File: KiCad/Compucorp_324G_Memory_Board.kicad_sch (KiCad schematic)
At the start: 1 part, among them J10 Memory Interboard

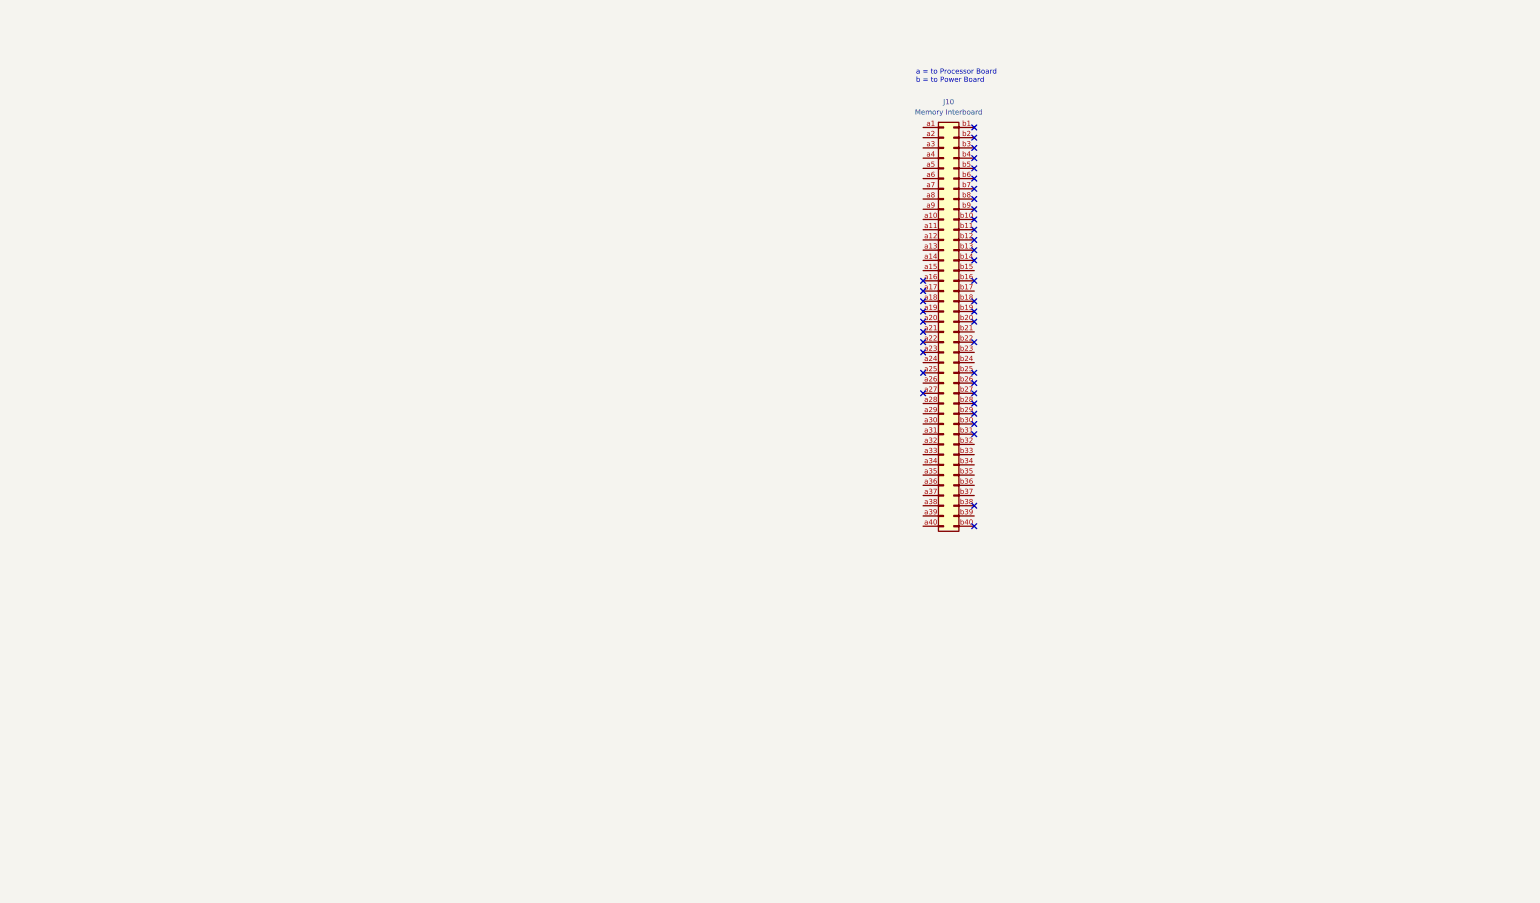
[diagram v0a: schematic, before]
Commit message: Started Memory Board schematic
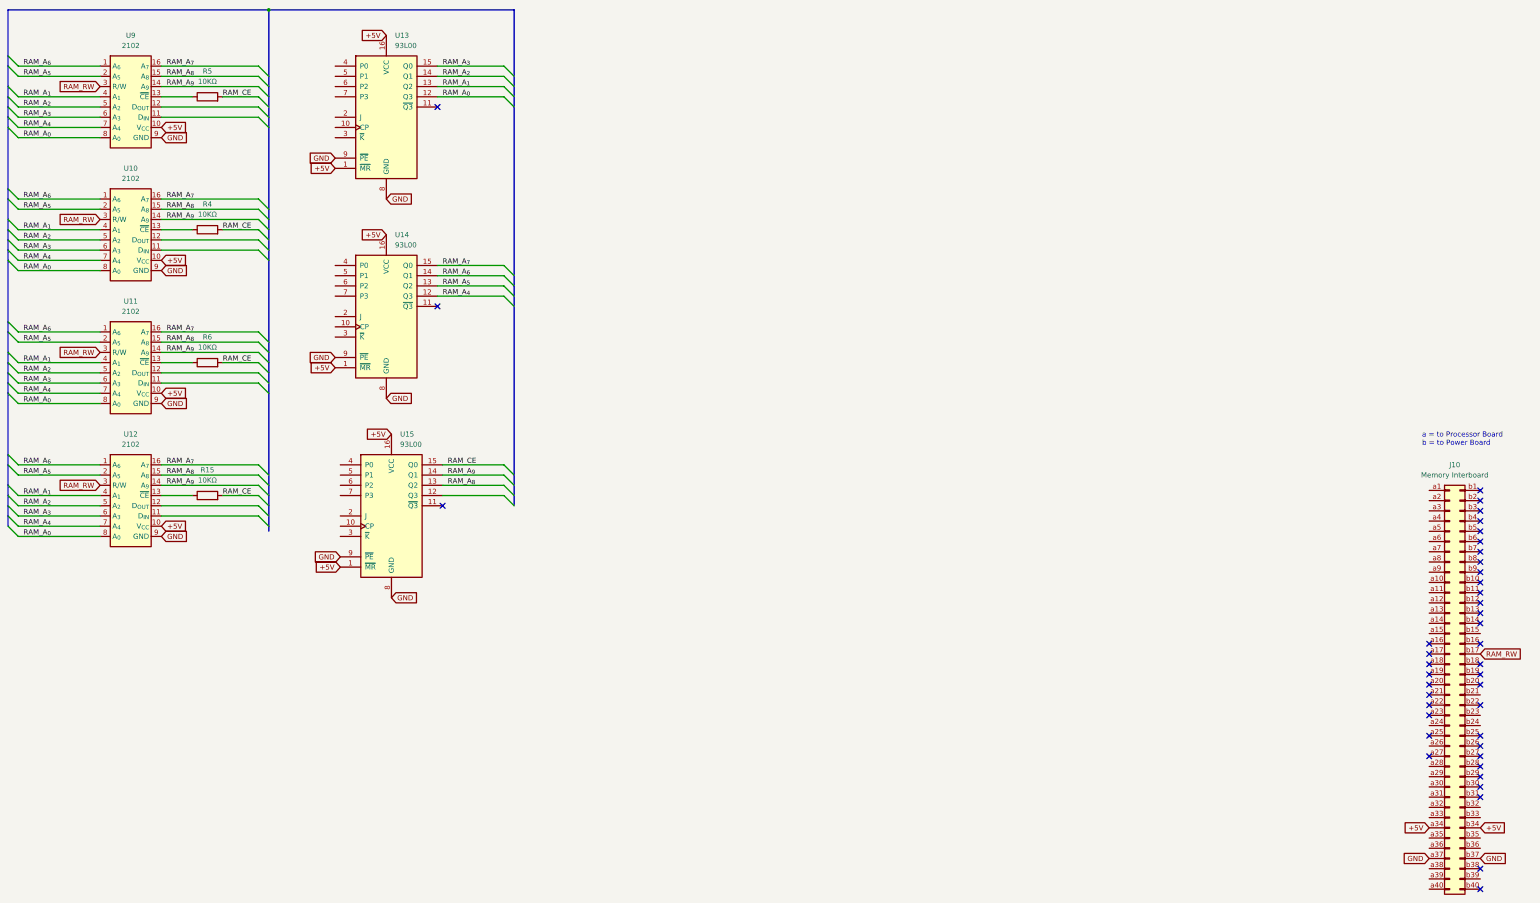
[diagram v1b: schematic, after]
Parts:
- added R15, R4, R5, R6: 10KΩ, symbol Device:R
- added U10, U11, U12, U9: 2102, symbol Compucorp_324G_Scientist:C2102
- added U13, U14, U15: 93L00, symbol 74xx:74LS195
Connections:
- net +5V: now reaches J10.a34 (Pin_a34)
- net +5V: now also J10.b34 (Pin_b34), U10.10 (V_{CC}), U11.10 (V_{CC}), U12.10 (V_{CC}), U13.1 (~{MR}), U13.16 (VCC), U14.1 (~{MR}), U14.16 (VCC), U15.1 (~{MR}), U15.16 (VCC), U9.10 (V_{CC})
- net GND: now reaches J10.a37 (Pin_a37)
- net GND: now also J10.b37 (Pin_b37), U10.9 (GND), U11.9 (GND), U12.9 (GND), U13.8 (GND), U13.9 (~{PE}), U14.8 (GND), U14.9 (~{PE}), U15.8 (GND), U15.9 (~{PE}), U9.9 (GND)
- net RAM_RW: now reaches J10.b17 (Pin_b17)
- net RAM_RW: now also U10.3 (R/W), U11.3 (R/W), U12.3 (R/W), U9.3 (R/W)
- new net: R5.1, U9.13 (~{CE})
- new net: R4.1, U10.13 (~{CE})
- new net: R15.1, U12.13 (~{CE})
- new net: R6.1, U11.13 (~{CE})
- new net RAM_A_{0}: U10.8 (A_{0}), U11.8 (A_{0}), U12.8 (A_{0}), U13.12 (Q3), U9.8 (A_{0})
- new net RAM_A_{1}: U10.4 (A_{1}), U11.4 (A_{1}), U12.4 (A_{1}), U13.13 (Q2), U9.4 (A_{1})
- new net RAM_A_{2}: U10.5 (A_{2}), U11.5 (A_{2}), U12.5 (A_{2}), U13.14 (Q1), U9.5 (A_{2})
- new net RAM_A_{3}: U10.6 (A_{3}), U11.6 (A_{3}), U12.6 (A_{3}), U13.15 (Q0), U9.6 (A_{3})
- new net RAM_A_{4}: U10.7 (A_{4}), U11.7 (A_{4}), U12.7 (A_{4}), U14.12 (Q3), U9.7 (A_{4})
- new net RAM_A_{5}: U10.2 (A_{5}), U11.2 (A_{5}), U12.2 (A_{5}), U14.13 (Q2), U9.2 (A_{5})
- new net RAM_A_{6}: U10.1 (A_{6}), U11.1 (A_{6}), U12.1 (A_{6}), U14.14 (Q1), U9.1 (A_{6})
- new net RAM_A_{7}: U10.16 (A_{7}), U11.16 (A_{7}), U12.16 (A_{7}), U14.15 (Q0), U9.16 (A_{7})
- new net RAM_A_{8}: U10.15 (A_{8}), U11.15 (A_{8}), U12.15 (A_{8}), U15.13 (Q2), U9.15 (A_{8})
- new net RAM_A_{9}: U10.14 (A_{9}), U11.14 (A_{9}), U12.14 (A_{9}), U15.14 (Q1), U9.14 (A_{9})
- new net RAM_CE: R15.2, R4.2, R5.2, R6.2, U15.15 (Q0)
- no-connect marks 38 -> 41
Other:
- company: (none) -> Brett Hallen
- title: (none) -> Compucorp 300-Series Memory Board
- moved on the sheet: J10

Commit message: Memory board updates
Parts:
- added D10, D11, D12, D9: D, symbol Device:D
- added Q1, Q2, Q3, Q4: 2N4403, symbol Simulation_SPICE:PNP
- added R16, R21, R24, R27: 3.3KΩ, symbol Device:R
- added R17, R20, R23, R26: 1KΩ, symbol Device:R
- added R18, R19, R22, R25: 10KΩ, symbol Device:R
- added U16: 74L75, symbol 74xx:74LS75
- added U17: TMC1871 (TCL03), symbol Compucorp_324G_Scientist:TMC1871
- added U18: 8KR11A, symbol Compucorp_324G_Scientist:ROM
- added U19: 8KR029, symbol Compucorp_324G_Scientist:ROM
- added U20: 8KR218, symbol Compucorp_324G_Scientist:ROM
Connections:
- net +5V: now also Q1.3 (E), Q2.3 (E), Q3.3 (E), Q4.3 (E), R17.2, R20.2, R23.2, R26.2, U16.5 (VCC), U17.1 (Pin_1), U18.1, U19.1, U20.1
- net GND: now also D10.2 (A), D11.2 (A), D12.2 (A), D9.2 (A), U16.12 (GND)
- net TCL03_24: now reaches U14.4 (P0)
- net TCL03_24: now also U17.24 (Pin_24), U18.11, U19.11, U20.11
- net TCL03_25: now reaches U14.5 (P1)
- net TCL03_25: now also U17.25 (Pin_25), U18.10, U19.10, U20.10
- net TCL03_26: now reaches U14.6 (P2)
- net TCL03_26: now also U17.26 (Pin_26), U18.9, U19.9, U20.9
- net TCL03_21: now reaches U14.7 (P3)
- net TCL03_21: now also U17.21 (Pin_21)
- net RAM_D_{IN1}: now reaches U9.11 (D_{IN})
- net RAM_D_{IN1}: now also U16.8 (~{Q3})
- net RAM_D_{OUT1}: now reaches U9.12 (D_{OUT})
- net RAM_D_{OUT1}: now also R21.1
- net TCL03_28: now reaches U13.4 (P0)
- net TCL03_28: now also U17.28 (Pin_28), U18.7, U19.7, U20.7
- net TCL03_29: now reaches U13.5 (P1)
- net TCL03_29: now also U17.29 (Pin_29), U18.6, U19.6, U20.6
- net TCL03_30: now reaches U13.6 (P2)
- net TCL03_30: now also U17.30 (Pin_30), U18.5, U19.5, U20.5
- net TCL03_08: now reaches U13.7 (P3)
- net TCL03_08: now also U17.8 (Pin_8), U18.4, U19.4, U20.4
- net IB_10: now reaches J10.a10 (Pin_a10)
- net IB_10: now also R18.1, U18.21, U19.21, U20.21
- net IB_02: now reaches J10.a2 (Pin_a2)
- net IB_02: now also U17.3 (Pin_3)
- net IB_28: now reaches J10.a28 (Pin_a28)
- net IB_28: now also U16.2 (D0)
- net IB_29: now reaches J10.a29 (Pin_a29)
- net IB_29: now also U16.3 (D1)
- net IB_30: now reaches J10.a30 (Pin_a30)
- net IB_30: now also U16.6 (D2)
- net IB_31: now reaches J10.a31 (Pin_a31)
- net IB_31: now also U16.7 (D3)
- net IB_33: now reaches J10.a33 (Pin_a33)
- net IB_33: now also J10.b33 (Pin_b33), U16.13 (E01), U16.4 (E23)
- net -25V: now reaches J10.a36 (Pin_a36)
- net -25V: now also J10.b36 (Pin_b36), U18.19, U19.19, U20.19
- net IB_40: now reaches J10.a40 (Pin_a40)
- net IB_40: now also U17.2 (Pin_2)
- net IB_07: now reaches J10.a7 (Pin_a7)
- net IB_07: now also R25.1, U18.22, U19.22, U20.22
- net IB_08: now reaches J10.a8 (Pin_a8)
- net IB_08: now also R22.1, U18.23, U19.23, U20.23
- net IB_09: now reaches J10.a9 (Pin_a9)
- net IB_09: now also R19.1, U18.20, U19.20, U20.20
- net IB_23: now reaches J10.b23 (Pin_b23)
- net IB_23: now also U18.3, U19.3, U20.3
- net RAM_D_{IN2}: now reaches U10.11 (D_{IN})
- net RAM_D_{IN2}: now also U16.11 (~{Q2})
- net RAM_D_{OUT2}: now reaches U10.12 (D_{OUT})
- net RAM_D_{OUT2}: now also R16.1
- net RAM_D_{IN3}: now reaches U11.11 (D_{IN})
- net RAM_D_{IN3}: now also U16.14 (~{Q1})
- net RAM_D_{OUT3}: now reaches U11.12 (D_{OUT})
- net RAM_D_{OUT3}: now also R27.1
- net RAM_D_{IN4}: now reaches U12.11 (D_{IN})
- net RAM_D_{IN4}: now also U16.1 (~{Q0})
- net RAM_D_{OUT4}: now reaches U12.12 (D_{OUT})
- net RAM_D_{OUT4}: now also R24.1
- net TCL03_11: now reaches U15.4 (P0)
- net TCL03_11: now also U17.11 (Pin_11)
- net TCL03_18: now reaches U15.5 (P1)
- net TCL03_18: now also U17.18 (Pin_18), U18.17, U19.17, U20.17
- net TCL03_23: now reaches U15.6 (P2)
- net TCL03_23: now also U17.23 (Pin_23), U18.12, U19.12, U20.12
- new net: D9.1 (K), Q2.1 (C), R18.2
- new net: Q3.2 (B), R23.1, R24.2
- new net: Q1.2 (B), R20.1, R21.2
- new net: Q4.2 (B), R26.1, R27.2
- new net: D10.1 (K), Q1.1 (C), R19.2
- new net: Q2.2 (B), R16.2, R17.1
- new net: D11.1 (K), Q3.1 (C), R22.2
- new net: D12.1 (K), Q4.1 (C), R25.2
- new net TCL03_09: U17.9 (Pin_9), U18.27, U19.27, U20.27
- new net TCL03_10: U17.10 (Pin_10), U18.26, U19.26, U20.26
- new net TCL03_13: U17.13 (Pin_13), U18.25, U19.25, U20.25
- new net TCL03_14: U17.14 (Pin_14), U18.24, U19.24, U20.24
- new net TCL03_16: U17.16 (Pin_16), U18.28, U19.28, U20.28
- new net TCL03_17: U17.17 (Pin_17), U18.18, U19.18, U20.18
- new net TCL03_19: U17.19 (Pin_19)
- new net TCL03_20: U17.20 (Pin_20)
- new net TCL03_27: U17.27 (Pin_27), U18.8, U19.8, U20.8
- new net TCL03_35: U17.35 (Pin_35), U18.2, U19.2, U20.2
- no-connect marks 41 -> 67
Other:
- note added: "Huh?"
- moved on the sheet: R15, R4, R5, R6

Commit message: Memory board updates
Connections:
- net TCL03_16 is gone; now on net -10V: U17.16 (Pin_16), U18.28, U19.28, U20.28
- net TCL03_35 is gone; now on net IB_32: U17.35 (Pin_35), U18.2, U19.2, U20.2
- net -25V: no longer U18.19, U19.19, U20.19
- net IB_02: now also U17.38 (Pin_38); no longer U17.3 (Pin_3)
- net IB_31: now also J10.b31 (Pin_b31)
- net IB_33: now also U17.37 (Pin_37)
- net IB_40: now also U17.39 (Pin_39); no longer U17.2 (Pin_2)
- net RAM_RW: now also J10.b23 (Pin_b23); no longer J10.b17 (Pin_b17)
- net IB_01: now reaches J10.a1 (Pin_a1)
- net IB_01: now also U17.33 (Pin_33)
- net IB_11: now reaches J10.a11 (Pin_a11)
- net IB_11: now also U17.34 (Pin_34)
- net TCL03_22: now reaches J10.a15 (Pin_a15)
- net TCL03_22: now also U17.22 (Pin_22)
- net IB_26: now reaches J10.a26 (Pin_a26)
- net IB_26: now also U17.32 (Pin_32)
- net IB_03: now reaches J10.a3 (Pin_a3)
- net IB_03: now also U17.3 (Pin_3)
- net IB_32: now reaches J10.a32 (Pin_a32)
- net IB_32: now also J10.b32 (Pin_b32)
- net -10V: now reaches J10.a35 (Pin_a35)
- net -10V: now also J10.b35 (Pin_b35)
- net IB_38: now reaches J10.a38 (Pin_a38)
- net IB_38: now also U17.40 (Pin_40)
- net IB_39: now reaches J10.a39 (Pin_a39)
- net IB_39: now also J10.b39 (Pin_b39), U17.31 (Pin_31)
- net IB_04: now reaches J10.a4 (Pin_a4)
- net IB_04: now also U17.4 (Pin_4)
- net IB_05: now reaches J10.a5 (Pin_a5)
- net IB_05: now also U17.6 (Pin_6)
- net IB_06: now reaches J10.a6 (Pin_a6)
- net IB_06: now also U17.7 (Pin_7)
- net IB_15: now reaches J10.b15 (Pin_b15)
- net IB_15: now also U17.2 (Pin_2)
- net TCL03_05: now reaches U17.5 (Pin_5)
- net TCL03_05: now also U18.19, U19.19, U20.19
- net IB_23 renamed IB_17
- net IB_17: now also J10.b17 (Pin_b17); no longer J10.b23 (Pin_b23)
- no-connect marks 67 -> 72
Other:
- note removed: "Huh?"
- moved on the sheet: U17

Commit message: Update Compucorp_324G_Memory_Board.kicad_sch
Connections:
- net TCL03_19 is gone; now on net IB_12: U17.19 (Pin_19)
- net TCL03_20 is gone; now on net IB_13: U17.20 (Pin_20)
- net TCL03_22 is gone; now on net IB_15: J10.a15 (Pin_a15), U17.22 (Pin_22)
- net TCL03_21: no longer U17.21 (Pin_21)
- net IB_12: now reaches J10.a12 (Pin_a12)
- net IB_13: now reaches J10.a13 (Pin_a13)
- net IB_14: now reaches J10.a14 (Pin_a14)
- net IB_14: now also U17.21 (Pin_21)
- no-connect marks 72 -> 71
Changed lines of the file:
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@@
 	)
 	(no_connect
-		(at 290.83 198.12)
-	)
-	(no_connect
 		(at 373.38 181.61)
 	)
@@
 	)
 	(bus_entry
-		(at 163.83 226.06)
-		(size 2.54 2.54)
-		(stroke
-			(width 0)
-			(type default)
-		)
-	)
-	(bus_entry
 		(at 163.83 223.52)
 		(size 2.54 2.54)
@@
 	)
 	(bus_entry
-		(at 163.83 228.6)
-		(size 2.54 2.54)
-		(stroke
-			(width 0)
-			(type default)
-		)
-	)
-	(bus_entry
 		(at 163.83 135.89)
 		(size 2.54 2.54)
@@
 	)
 	(bus_entry
-		(at 232.41 231.14)
-		(size 2.54 2.54)
-		(stroke
-			(width 0)
-			(type default)
-		)
-	)
-	(bus_entry
 		(at 232.41 128.27)
 		(size 2.54 2.54)
@@
 		)
 	)
-	(wire
-		(pts
-			(xy 166.37 231.14) (xy 184.15 231.14)
-		)
-		(stroke
-			(width 0)
-			(type default)
-		)
-	)
 	(bus
 		(pts
@@
 		)
 	)
-	(bus
-		(pts
-			(xy 163.83 223.52) (xy 163.83 226.06)
-		)
-		(stroke
-			(width 0)
-			(type default)
-		)
-	)
 	(wire
 		(pts
@@
 		)
 	)
-	(bus
-		(pts
-			(xy 163.83 226.06) (xy 163.83 228.6)
-		)
-		(stroke
-			(width 0)
-			(type default)
-		)
-	)
 	(wire
 		(pts
@@
 	(wire
 		(pts
-			(xy 166.37 228.6) (xy 184.15 228.6)
-		)
-		(stroke
-			(width 0)
-			(type default)
-		)
-	)
-	(wire
-		(pts
 			(xy 127 80.01) (xy 161.29 80.01)
 		)
@@
 		)
 	)
-	(bus
-		(pts
-			(xy 234.95 228.6) (xy 234.95 233.68)
-		)
-		(stroke
-			(width 0)
-			(type default)
-		)
-	)
 	(wire
 		(pts
@@
 		)
 	)
-	(wire
-		(pts
-			(xy 209.55 231.14) (xy 232.41 231.14)
-		)
-		(stroke
-			(width 0)
-			(type default)
-		)
-	)
 	(bus
 		(pts
@@
 		)
 	)
-	(label "TCL03_20"
-		(at 166.37 231.14 0)
-		(effects
-			(font
-				(size 1.27 1.27)
-			)
-			(justify left bottom)
-		)
-	)
 	(label "TCL03_25"
 		(at 168.91 99.06 0)
@@
 		)
 	)
-	(label "TCL03_19"
-		(at 166.37 228.6 0)
-		(effects
-			(font
-				(size 1.27 1.27)
-			)
-			(justify left bottom)
-		)
-	)
 	(label "RAM_D_{OUT2}"
 		(at 102.87 233.68 180)
@@
 		)
 	)
-	(label "TCL03_21"
-		(at 222.25 231.14 0)
-		(effects
-			(font
-				(size 1.27 1.27)
-			)
-			(justify left bottom)
-		)
-	)
 	(label "TCL03_29"
 		(at 91.44 33.02 0)
@@
 		)
 	)
+	(global_label "IB_14"
+		(shape input)
+		(at 209.55 231.14 0)
+		(fields_autoplaced yes)
+		(effects
+			(font
+				(size 1.27 1.27)
+			)
+			(justify left)
+		)
+		(property "Intersheetrefs" "${INTERSHEET_REFS}"
+			(at 217.7966 231.14 0)
+			(effects
+				(font
+					(size 1.27 1.27)
+				)
+				(justify left)
+				(hide yes)
+			)
+		)
+	)
 	(global_label "GND"
 		(shape input)
@@
 		)
 	)
+	(global_label "IB_14"
+		(shape input)
+		(at 373.38 168.91 180)
+		(fields_autoplaced yes)
+		(effects
+			(font
+				(size 1.27 1.27)
+			)
+			(justify right)
+		)
+		(property "Intersheetrefs" "${INTERSHEET_REFS}"
+			(at 365.1334 168.91 0)
+			(effects
+				(font
+					(size 1.27 1.27)
+				)
+				(justify right)
+				(hide yes)
+			)
+		)
+	)
 	(global_label "GND"
 		(shape input)
@@
 		)
 	)
+	(global_label "IB_13"
+		(shape input)
+		(at 184.15 231.14 180)
+		(fields_autoplaced yes)
+		(effects
+			(font
+				(size 1.27 1.27)
+			)
+			(justify right)
+		)
+		(property "Intersheetrefs" "${INTERSHEET_REFS}"
+			(at 175.9034 231.14 0)
+			(effects
+				(font
+					(size 1.27 1.27)
+				)
+				(justify right)
+				(hide yes)
+			)
+		)
+	)
 	(global_label "-10V"
 		(shape input)
@@
 		)
 	)
-	(global_label "TCL03_22"
-		(shape input)
-		(at 209.55 228.6 0)
-		(fields_autoplaced yes)
-		(effects
-			(font
-				(size 1.27 1.27)
-			)
-			(justify left)
-		)
-		(property "Intersheetrefs" "${INTERSHEET_REFS}"
-			(at 221.6065 228.6 0)
-			(effects
-				(font
-					(size 1.27 1.27)
-				)
-				(justify left)
-				(hide yes)
-			)
-		)
-	)
 	(global_label "IB_03"
 		(shape input)
@@
 		)
 	)
+	(global_label "IB_15"
+		(shape input)
+		(at 373.38 171.45 180)
+		(fields_autoplaced yes)
+		(effects
+			(font
+				(size 1.27 1.27)
+			)
+			(justify right)
+		)
+		(property "Intersheetrefs" "${INTERSHEET_REFS}"
+			(at 365.1334 171.45 0)
+			(effects
+				(font
+					(size 1.27 1.27)
+				)
+				(justify right)
+				(hide yes)
+			)
+		)
+	)
 	(global_label "IB_06"
 		(shape input)
@@
 		)
 	)
+	(global_label "IB_12"
+		(shape input)
+		(at 373.38 163.83 180)
+		(fields_autoplaced yes)
+		(effects
+			(font
+				(size 1.27 1.27)
+			)
+			(justify right)
+		)
+		(property "Intersheetrefs" "${INTERSHEET_REFS}"
+			(at 365.1334 163.83 0)
+			(effects
+				(font
+					(size 1.27 1.27)
+				)
+				(justify right)
+				(hide yes)
+			)
+		)
+	)
 	(global_label "IB_39"
 		(shape input)
@@
 		)
 	)
+	(global_label "IB_13"
+		(shape input)
+		(at 373.38 166.37 180)
+		(fields_autoplaced yes)
+		(effects
+			(font
+				(size 1.27 1.27)
+			)
+			(justify right)
+		)
+		(property "Intersheetrefs" "${INTERSHEET_REFS}"
+			(at 365.1334 166.37 0)
+			(effects
+				(font
+					(size 1.27 1.27)
+				)
+				(justify right)
+				(hide yes)
+			)
+		)
+	)
 	(global_label "IB_07"
 		(shape input)
@@
 		)
 	)
-	(global_label "TCL03_22"
+	(global_label "IB_08"
 		(shape input)
-		(at 373.38 171.45 180)
+		(at 45.72 196.85 0)
 		(fields_autoplaced yes)
 		(effects
@@
 				(size 1.27 1.27)
 			)
-			(justify right)
+			(justify left)
 		)
 		(property "Intersheetrefs" "${INTERSHEET_REFS}"
-			(at 361.3235 171.45 0)
+			(at 53.9666 196.85 0)
 			(effects
 				(font
 					(size 1.27 1.27)
 				)
-				(justify right)
+				(justify left)
 				(hide yes)
 			)
 		)
 	)
-	(global_label "IB_08"
+	(global_label "IB_09"
 		(shape input)
-		(at 45.72 196.85 0)
+		(at 129.54 185.42 180)
 		(fields_autoplaced yes)
 		(effects
@@
 				(size 1.27 1.27)
 			)
-			(justify left)
+			(justify right)
 		)
 		(property "Intersheetrefs" "${INTERSHEET_REFS}"
-			(at 53.9666 196.85 0)
+			(at 121.2934 185.42 0)
 			(effects
 				(font
 					(size 1.27 1.27)
 				)
-				(justify left)
+				(justify right)
 				(hide yes)
 			)
 		)
 	)
-	(global_label "IB_09"
+	(global_label "+5V"
 		(shape input)
-		(at 129.54 185.42 180)
+		(at 101.6 105.41 180)
 		(fields_autoplaced yes)
 		(effects
@@
 		)
 		(property "Intersheetrefs" "${INTERSHEET_REFS}"
-			(at 121.2934 185.42 0)
+			(at 94.7443 105.41 0)
 			(effects
 				(font
@@
 		)
 	)
-	(global_label "+5V"
+	(global_label "IB_12"
 		(shape input)
-		(at 101.6 105.41 180)
+		(at 184.15 228.6 180)
 		(fields_autoplaced yes)
 		(effects
@@
 		)
 		(property "Intersheetrefs" "${INTERSHEET_REFS}"
-			(at 94.7443 105.41 0)
+			(at 175.9034 228.6 0)
 			(effects
 				(font
@@
 			(effects
 				(font
+					(size 1.27 1.27)
+				)
+				(justify left)
+				(hide yes)
+			)
+		)
+	)
+	(global_label "IB_15"
+		(shape input)
+		(at 209.55 228.6 0)
+		(fields_autoplaced yes)
+		(effects
+			(font
+				(size 1.27 1.27)
+			)
+			(justify left)
+		)
+		(property "Intersheetrefs" "${INTERSHEET_REFS}"
+			(at 217.7966 228.6 0)
+			(effects
+				(font

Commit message: Update Compucorp_324G_Memory_Board.kicad_sch
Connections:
- net +5V: now also R17.1, R20.1, R23.1, R26.1; no longer R17.2, R20.2, R23.2, R26.2
- net at Q3.2 (B), R24.2: now also R23.2; no longer R23.1
- net at Q1.2 (B), R21.2: now also R20.2; no longer R20.1
- net at Q4.2 (B), R27.2: now also R26.2; no longer R26.1
- net at Q2.2 (B), R16.2: no longer R17.1
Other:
- moved on the sheet: R17, R20, R23, R24, R26, R27
